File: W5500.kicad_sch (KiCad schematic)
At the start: 2 parts, among them J7 J1B1211CCD, U1 W5500

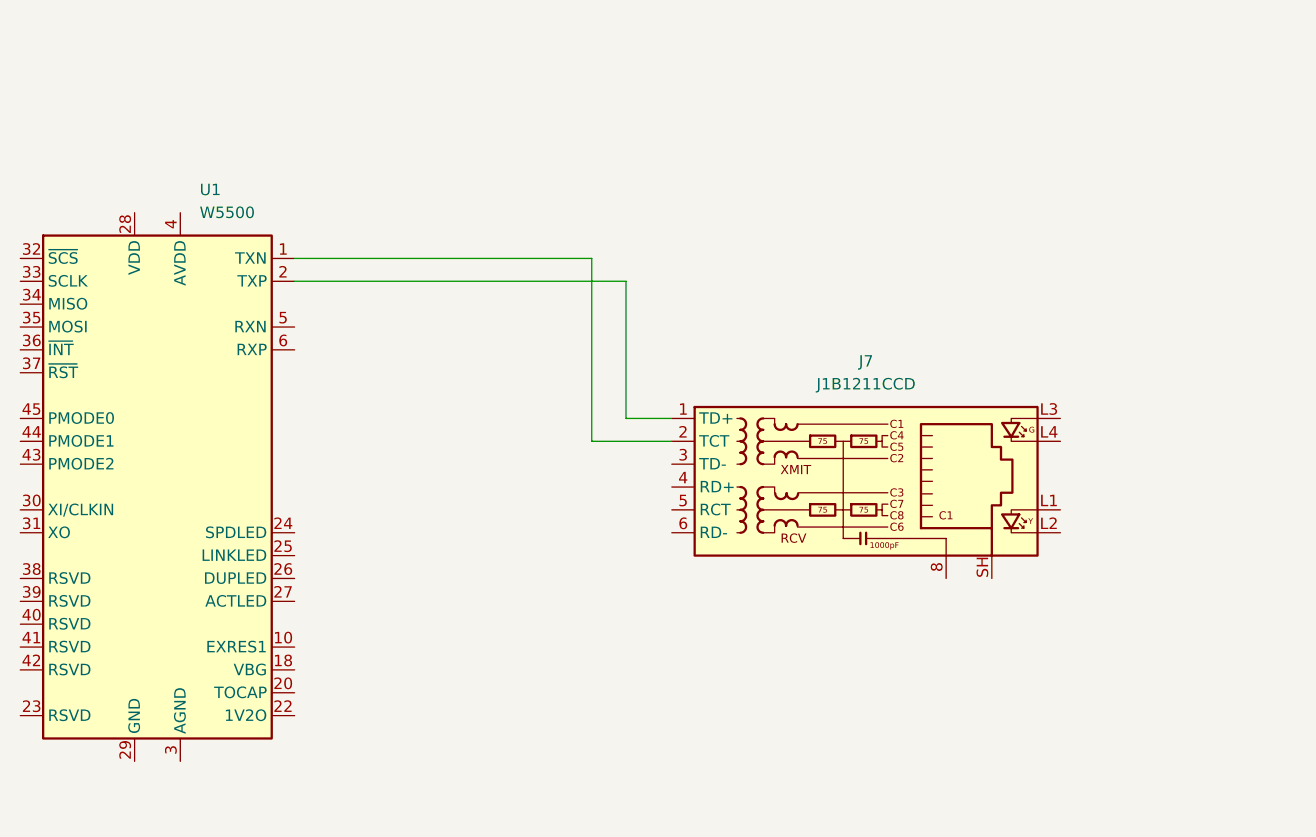
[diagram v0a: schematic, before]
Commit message: update: add modular jack
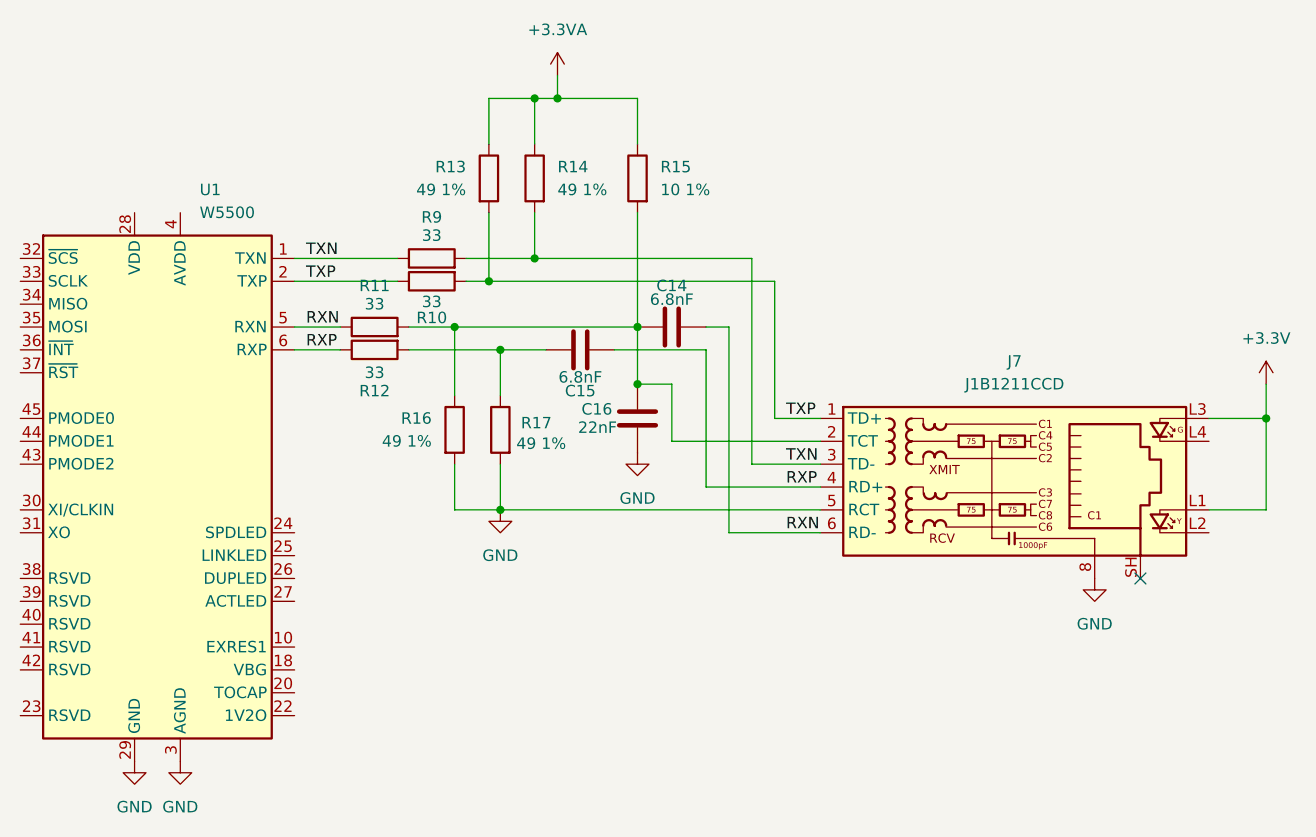
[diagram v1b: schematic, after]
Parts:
- added C14, C15: 6.8nF, Capacitor_SMD:C_0402_1005Metric_Pad0.74x0.62mm_HandSolder, symbol Device:C
- added C16: 22nF, Capacitor_SMD:C_0402_1005Metric_Pad0.74x0.62mm_HandSolder, symbol Device:C
- added R10, R11, R12, R9: 33, PCM_Resistor_SMD_AKL:R_0402_1005Metric_Pad0.72x0.64mm_HandSolder, symbol Device:R
- added R13, R14, R16, R17: 49 1%, PCM_Resistor_SMD_AKL:R_0402_1005Metric_Pad0.72x0.64mm_HandSolder, symbol Device:R
- added R15: 10 1%, PCM_Resistor_SMD_AKL:R_0402_1005Metric_Pad0.72x0.64mm_HandSolder, symbol Device:R
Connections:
- net TXP: now reaches J7.1 (TD+), U1.2 (TXP)
- net TXP: now also R10.1, R10.2, R13.2
- net at J7.2 (TCT): now also C14.1, C16.1, R11.2, R15.2, R16.1; no longer U1.1 (TXN)
- net TXN: now reaches J7.3 (TD-)
- net TXN: now also U1.1 (TXN), R14.2, R9.1, R9.2
- net RXP: now reaches J7.4 (RD+)
- net RXP: now also U1.6 (RXP), C15.2, R12.1
- net GND: now reaches J7.5 (RCT)
- net GND: now also J7.8, U1.14 (AGND), U1.16 (AGND), U1.19 (AGND), U1.29 (GND), U1.3 (AGND), U1.48 (AGND), U1.9 (AGND), C16.2, R16.2, R17.2
- net RXN: now reaches J7.6 (RD-)
- net RXN: now also U1.5 (RXN), C14.2, R11.1
- net +3.3V: now reaches J7.L1
- net +3.3V: now also J7.L3
- new net: C15.1, R12.2, R17.1
- new net +3.3VA: R13.1, R14.1, R15.1
- no-connect marks 0 -> 1
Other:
- moved on the sheet: J7
